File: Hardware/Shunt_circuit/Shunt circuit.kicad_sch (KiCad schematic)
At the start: 24 parts, among them J1 Conn_01x02, J2 Conn_01x02, J3 Conn_01x01, J4 Conn_01x01, J6 Conn_01x03, U1 INA238, U2 ISO1540, U3 ISO7710FQDRQ1

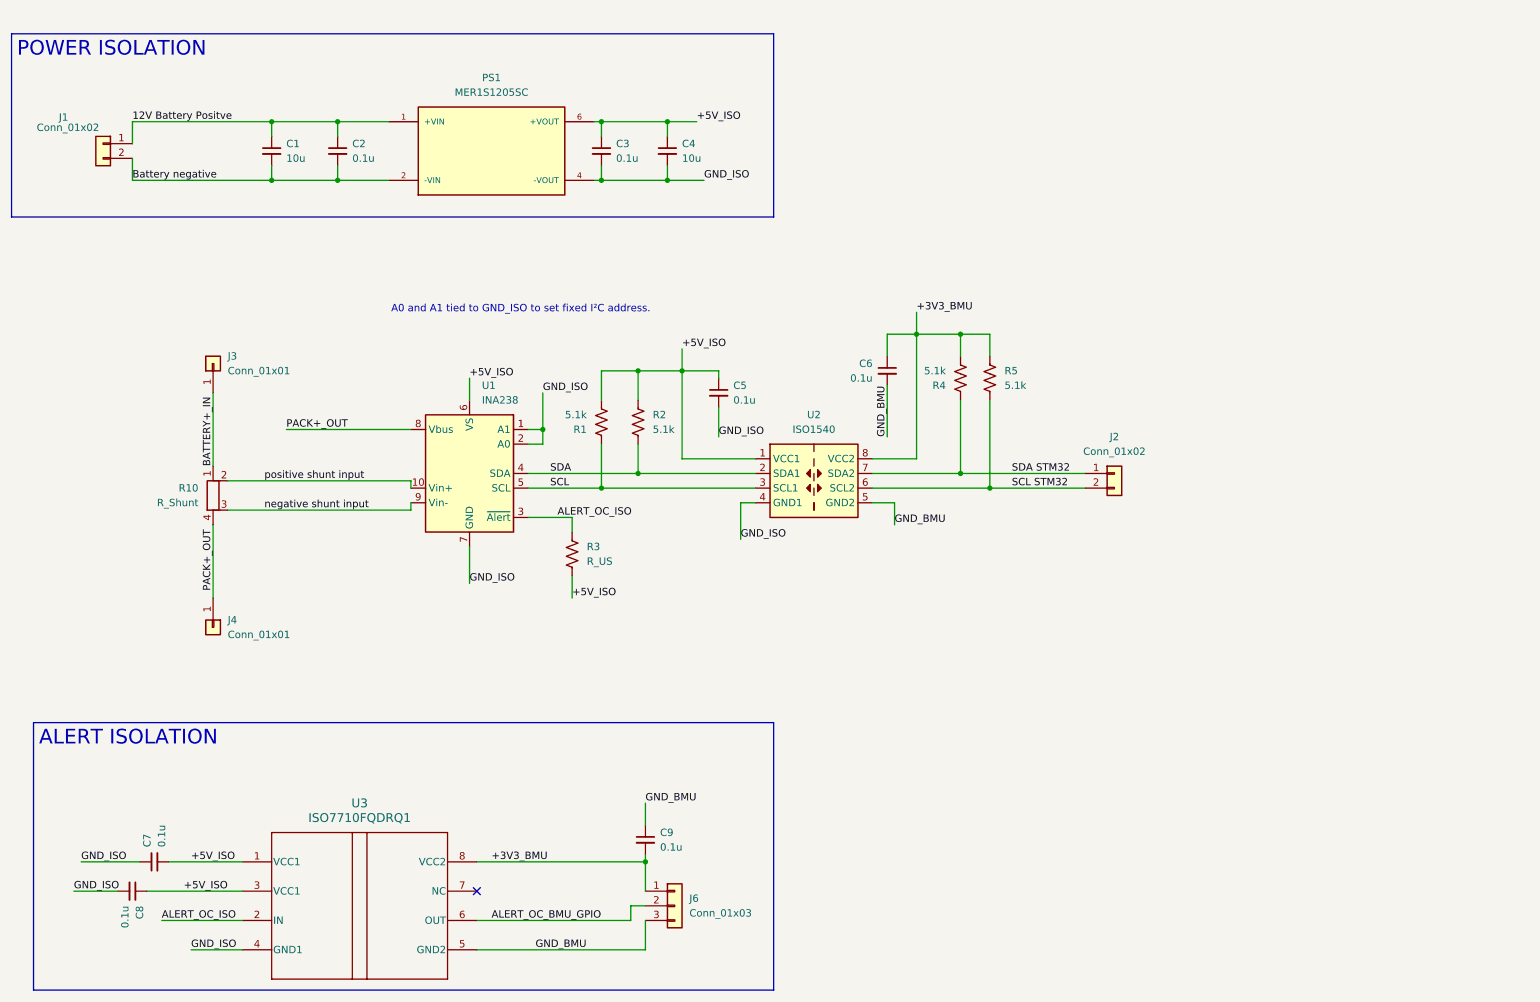
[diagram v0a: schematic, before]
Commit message: Update shunt circuit KiCad files
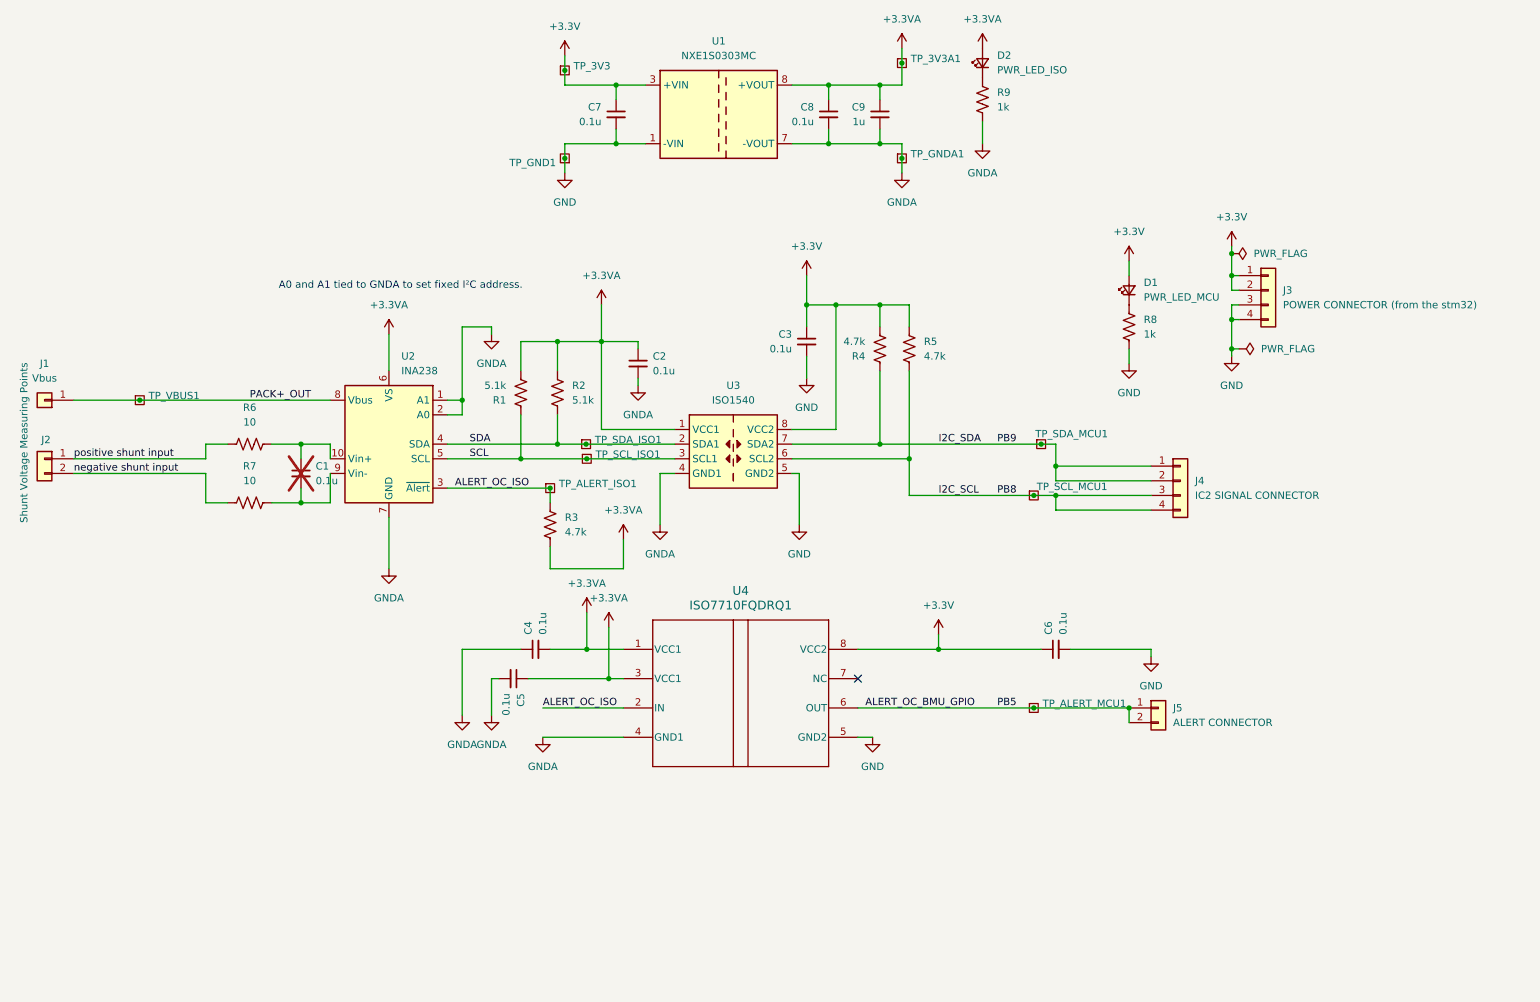
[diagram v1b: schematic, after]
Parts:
- removed J1: Conn_01x02, symbol Connector_Generic:Conn_01x02
- removed J3, J4: Conn_01x01, symbol Connector_Generic:Conn_01x01
- removed J6: Conn_01x03, symbol Connector_Generic:Conn_01x03
- removed PS1: MER1S1205SC, MER1S1205SC:CONV_MER1S1205SC, symbol MER1S1205SC:MER1S1205SC
- removed R10: R_Shunt, symbol Device:R_Shunt
- removed U1: INA238, Package_SO:VSSOP-10_3x3mm_P0.5mm, symbol Sensor_Energy:INA238
- removed U2: ISO1540, Package_SO:SOIC-8_3.9x4.9mm_P1.27mm, symbol Isolator:ISO1540
- removed U3: ISO7710FQDRQ1, ISO7710FQDRQ1(1):SOIC127P600X175-8N, symbol 2026-04-14_20-51-37:ISO7710FQDRQ1
- added D1: PWR_LED_MCU, LED_SMD:LED_0805_2012Metric, symbol Device:LED_Small
- added D2: PWR_LED_ISO, LED_SMD:LED_0805_2012Metric, symbol Device:LED_Small
- added J1: Vbus, Connector_PinHeader_2.54mm:PinHeader_1x01_P2.54mm_Vertical, symbol Connector_Generic:Conn_01x01
- added J3: POWER CONNECTOR (from the stm32), Connector_PinHeader_2.54mm:PinHeader_1x04_P2.54mm_Vertical, symbol Connector_Generic:Conn_01x04
- added J4: IC2 SIGNAL CONNECTOR, Connector_PinHeader_2.54mm:PinHeader_1x04_P2.54mm_Vertical, symbol Connector_Generic:Conn_01x04
- added J5: ALERT CONNECTOR, Connector_PinHeader_2.54mm:PinHeader_1x02_P2.54mm_Vertical, symbol Connector_Generic:Conn_01x02
- added R6, R7: 10, Resistor_SMD:R_0805_2012Metric, symbol Device:R_US
- added R8, R9: 1k, Resistor_SMD:R_0805_2012Metric, symbol Device:R_US
- added TP_3V3, TP_3V3A1, TP_ALERT_ISO1, TP_ALERT_MCU1, TP_GND1, TP_GNDA1, TP_SCL_ISO1, TP_SCL_MCU1, TP_SDA_ISO1, TP_SDA_MCU1, TP_VBUS1: TestPoint_Square, TestPoint:TestPoint_Pad_1.0x1.0mm, symbol Connector:TestPoint_Square
- added U1: NXE1S0303MC, Converter_DCDC:Converter_DCDC_Murata_NXExSxxxxMC_SMD, symbol Regulator_Switching:NXE1S0303MC
- added U2: INA238, Package_SO:TSSOP-10_3x3mm_P0.5mm, symbol Sensor_Energy:INA238
- added U3: ISO1540, Package_SO:SOIC-8_3.9x4.9mm_P1.27mm, symbol Isolator:ISO1540
- added U4: ISO7710FQDRQ1, footprints:D0008B_HV, symbol 2026-04-14_20-51-37:ISO7710FQDRQ1
- C1: value 10u -> 0.1u; footprint Capacitor_SMD:C_0402_1005Metric -> Capacitor_SMD:C_0805_2012Metric; now not fitted
- C2, C3, C5, C6, C7, C8: footprint Capacitor_SMD:C_0402_1005Metric -> Capacitor_SMD:C_0805_2012Metric
- C4: value 10u -> 0.1u; footprint Capacitor_SMD:C_0402_1005Metric -> Capacitor_SMD:C_0805_2012Metric
- C9: value 0.1u -> 1u; footprint Capacitor_SMD:C_0402_1005Metric -> Capacitor_SMD:C_0805_2012Metric
- J2: value Conn_01x02 -> Shunt Voltage Measuring Points; footprint (none) -> TerminalBlock_Phoenix:TerminalBlock_Phoenix_MKDS-1,5-2-5.08_1x02_P5.08mm_Horizontal
- R1, R2: footprint (none) -> Resistor_SMD:R_0805_2012Metric
- R3: value R_US -> 4.7k; footprint (none) -> Resistor_SMD:R_0805_2012Metric
- R4, R5: value 5.1k -> 4.7k; footprint (none) -> Resistor_SMD:R_0805_2012Metric
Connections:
- net ALERT_OC_BMU_GPIO: now also J5.1 (Pin_1), J5.2 (Pin_2), TP_ALERT_MCU1.1, U4.6 (OUT)
- net ALERT_OC_ISO: now also TP_ALERT_ISO1.1, U2.3 (~{Alert}), U4.2 (IN)
- net PACK+_OUT: now also J1.1 (Pin_1), TP_VBUS1.1, U2.8 (Vbus)
- net SCL: now also TP_SCL_ISO1.1, U2.5 (SCL), U3.3 (SCL1)
- net SDA: now also TP_SDA_ISO1.1, U2.4 (SDA), U3.2 (SDA1)
- net negative shunt input: now also J2.2 (Pin_2), R7.1
- net positive shunt input: now also J2.1 (Pin_1), R6.1
- net +3V3_BMU renamed +3.3V
- net +3.3V: now also C3.1, C7.1, D1.2 (A), J3.1 (Pin_1), J3.2 (Pin_2), TP_3V3.1, U1.3 (+VIN), U3.8 (VCC2), U4.8 (VCC2); no longer C9.2
- net +5V_ISO renamed +3.3VA
- net +3.3VA: now also C2.1, C4.2, C9.1, D2.2 (A), TP_3V3A1.1, U1.8 (+VOUT), U2.6 (VS), U3.1 (VCC1), U4.1 (VCC1), U4.3 (VCC1); no longer C3.1, C4.1, C7.2
- net 12V Battery Positve: no longer names the net of C1.1
- net 12V Battery Positve: now also R6.2, U2.10 (Vin+); no longer C2.1
- net Battery negative: no longer names the net of C1.2
- net Battery negative: now also R7.2, U2.9 (Vin-); no longer C2.2
- net GND_BMU renamed GND
- net GND: now also C3.2, C7.2, J3.3 (Pin_3), J3.4 (Pin_4), R8.2, TP_GND1.1, U1.1 (-VIN), U3.5 (GND2), U4.5 (GND2); no longer C9.1
- removed net GND_ISO: C3.2, C4.2, C5.2, C7.1, C8.2
- net SCL STM32 renamed I2C_SCL
- net I2C_SCL: now also J4.3 (Pin_3), J4.4 (Pin_4), TP_SCL_MCU1.1, U3.6 (SCL2); no longer J2.2 (Pin_2)
- net SDA STM32 renamed I2C_SDA
- net I2C_SDA: now also J4.1 (Pin_1), J4.2 (Pin_2), TP_SDA_MCU1.1, U3.7 (SDA2); no longer J2.1 (Pin_1)
- new net: D2.1 (K), R9.1
- new net: D1.1 (K), R8.1
- new net GNDA: C2.2, C4.1, C5.2, C8.2, C9.2, R9.2, TP_GNDA1.1, U1.7 (-VOUT), U2.1 (A1), U2.2 (A0), U2.7 (GND), U3.4 (GND1), U4.4 (GND1)
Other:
- note added: "A0 and A1 tied to GNDA to set fixed I²C address."
- note removed: "A0 and A1 tied to GND_ISO to set fixed I²C address."
